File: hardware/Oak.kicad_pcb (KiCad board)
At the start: 2 copper layers, 47 parts, among them J1 18650 Battery holder, J2 USB_B_Micro, J3 Conn_Coaxial, J4 Conn_ARM_JTAG_SWD_10, J5 Conn_01x12_Male, J6 Conn_01x12_Male, SW1 SW_SPDT, SW2 SW_Push, U1 AP2112, U2 ATSAMD21, U3 MCP7383, U4 PA1010D, U5 RFM95, U6 Waveshare_1in54_epaper

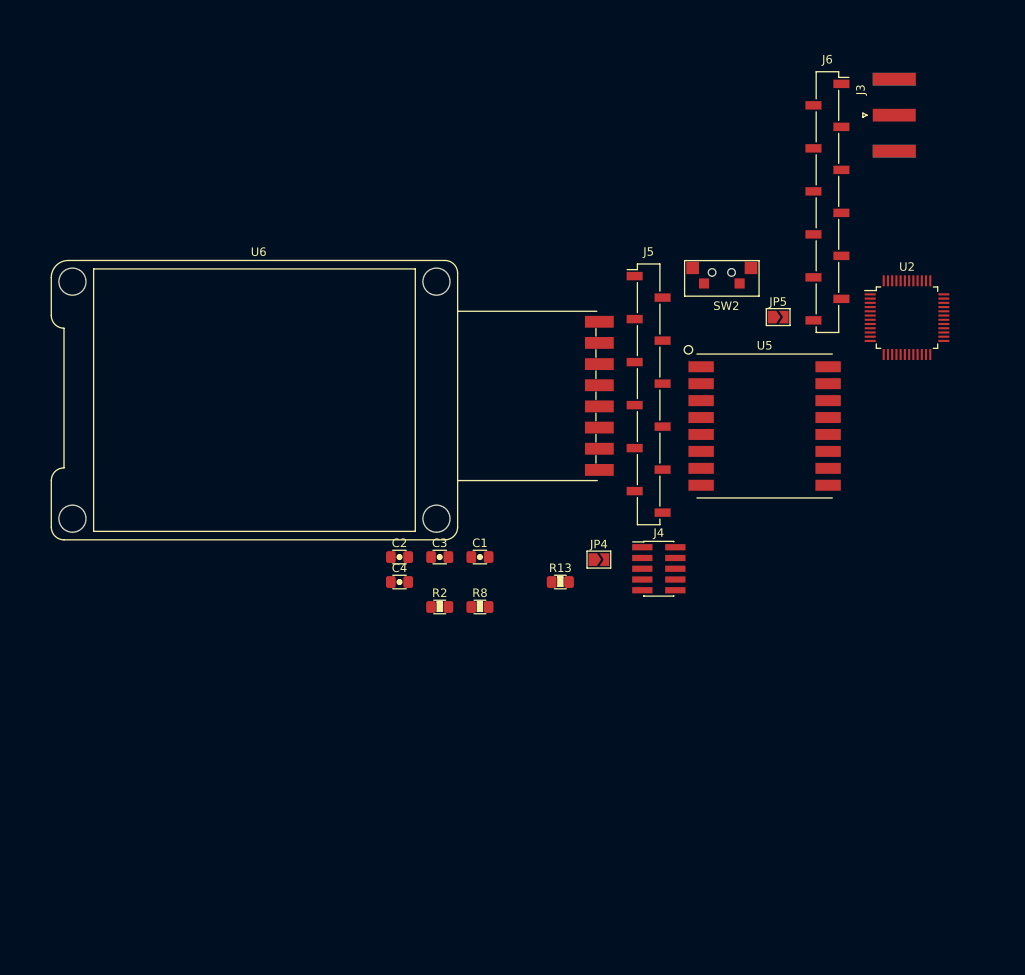
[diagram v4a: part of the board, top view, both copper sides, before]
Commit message: feat: move logical block lora components into a seperate block
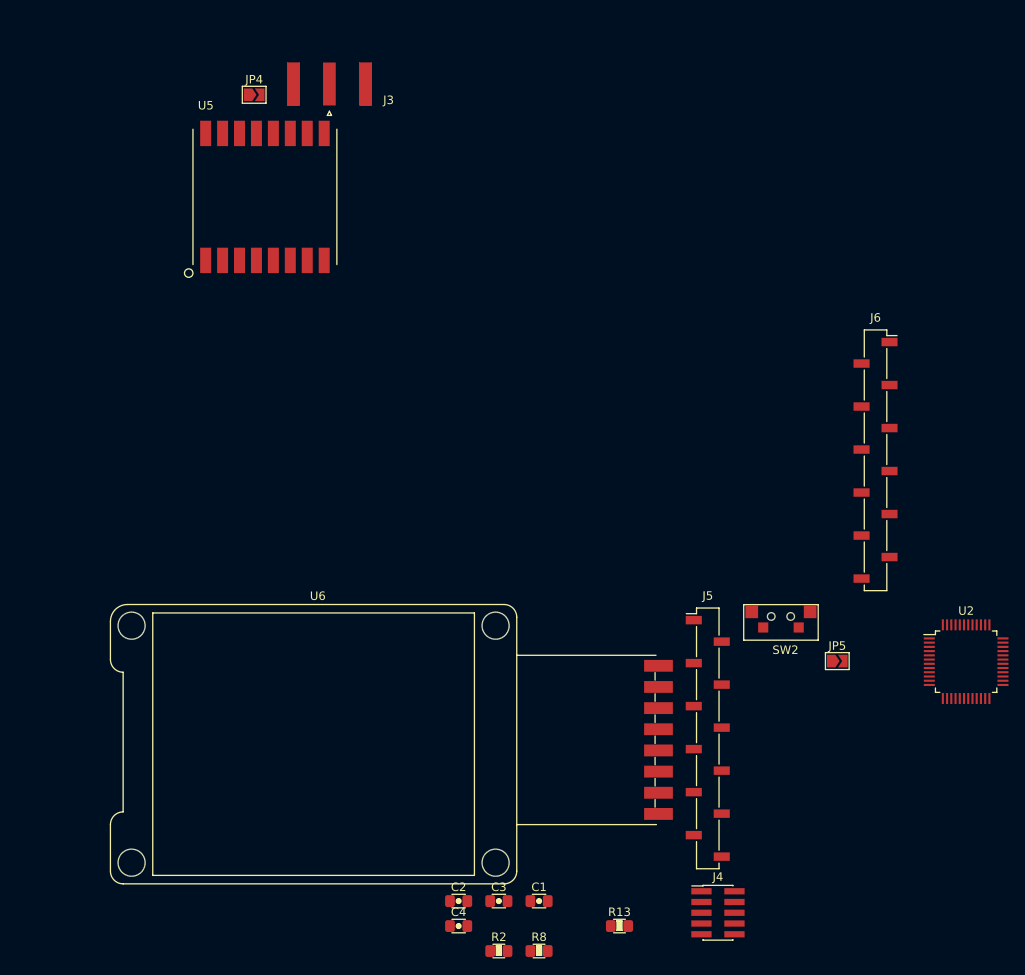
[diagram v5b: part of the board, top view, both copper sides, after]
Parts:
- moved JP4 68.4 mm to (132.1, 53.3)
- moved J3 66.8 mm to (141.0, 52.1), turned to 90 degrees
- moved U5 64.9 mm to (133.3, 65.4), turned to 90 degrees
- moved R2 41.2 mm to (161.0, 154.5)
- moved R8 41.2 mm to (165.7, 154.5)
- moved C1 41.2 mm to (165.7, 148.6)
- moved C2 41.2 mm to (156.2, 148.6)
- moved C3 41.2 mm to (161.0, 148.6)
- moved J4 41.2 mm to (186.9, 150.0)
- moved JP5 41.2 mm to (201.0, 120.2)
- moved SW2 41.2 mm to (194.3, 115.0)
- moved U2 41.2 mm to (216.2, 120.3)
- moved J5 41.2 mm to (185.7, 129.4)
- moved U6 41.2 mm to (139.6, 129.6)
- moved C4 41.2 mm to (156.2, 151.5)
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
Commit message: feat: move logical block eink components into a seperate block
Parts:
- moved U6 126.1 mm to (265.4, 121.9)
- moved JP5 93.6 mm to (293.4, 135.3)
- moved J1 18.5 mm to (75.6, 28.6)

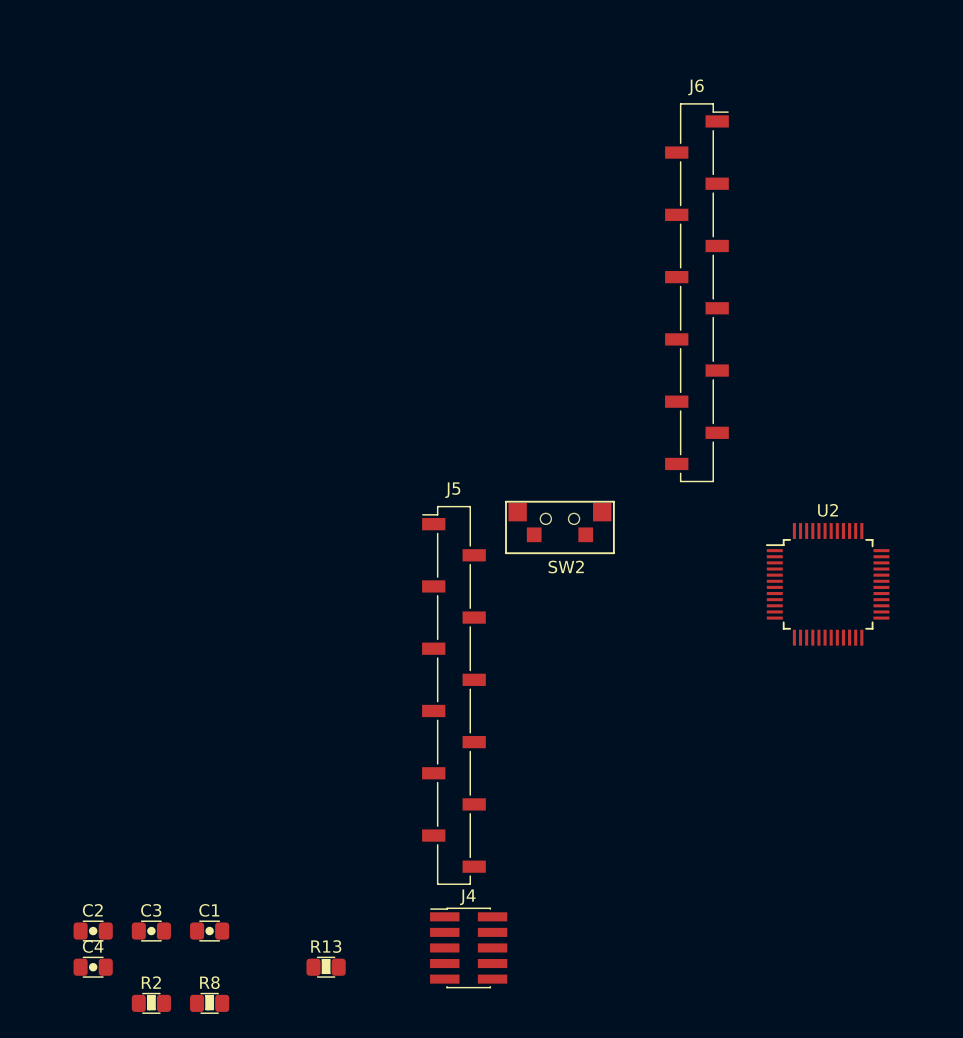
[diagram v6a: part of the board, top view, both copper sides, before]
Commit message: feat: move logical block mcu components into a seperate block
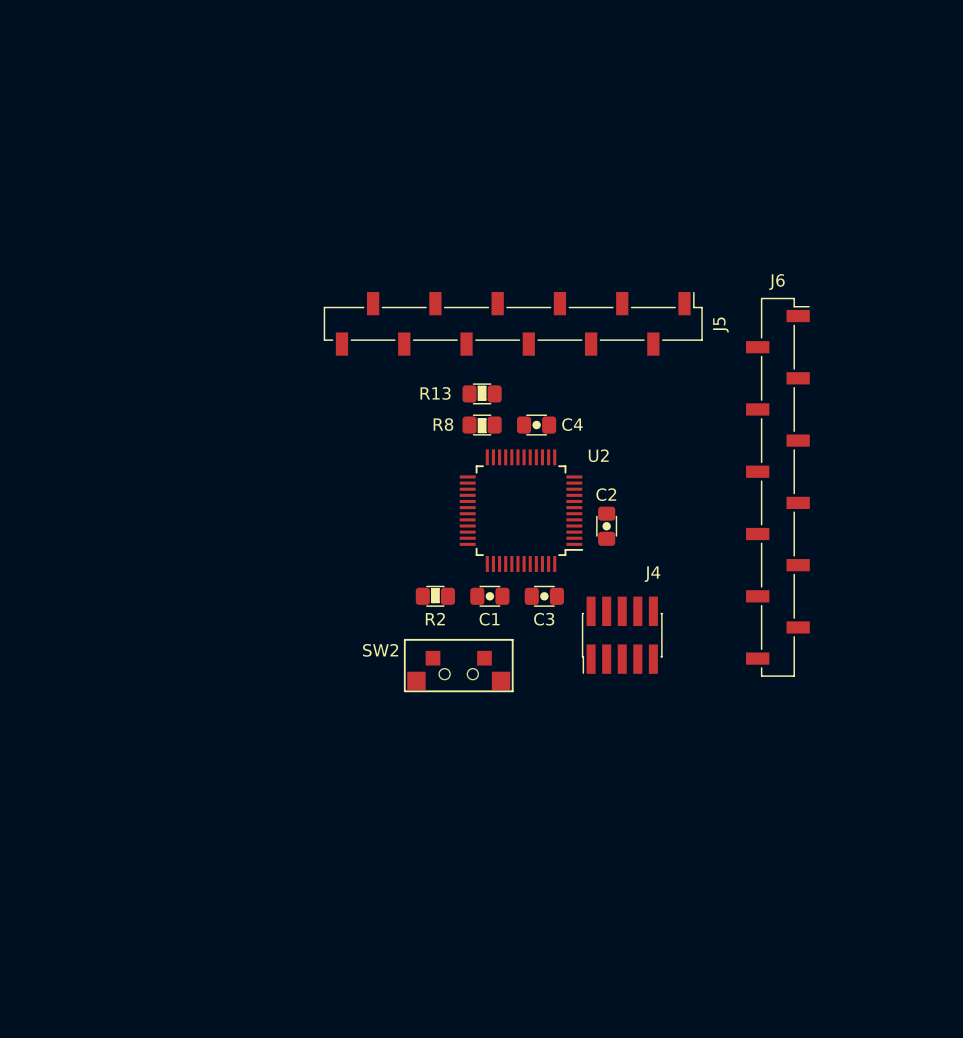
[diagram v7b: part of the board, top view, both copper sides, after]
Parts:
- moved C4 57.1 mm to (192.4, 107.3), turned to 180 degrees
- moved C2 53.3 mm to (198.1, 115.6), turned to 270 degrees
- moved R8 52.1 mm to (188.0, 107.3), turned to 180 degrees
- moved R13 48.5 mm to (188.0, 104.8)
- moved C3 42.1 mm to (193.0, 121.3)
- moved R2 40.5 mm to (184.2, 121.3)
- moved C1 35.6 mm to (188.6, 121.3)
- moved J5 30.7 mm to (190.5, 99.1), turned to 270 degrees
- moved J4 28.4 mm to (199.4, 124.5), turned to 90 degrees
- moved U2 25.8 mm to (191.1, 114.3), turned to 180 degrees
- moved J6 17.2 mm to (212.1, 112.4)
- moved SW2 15.1 mm to (186.1, 127.6), turned to 180 degrees

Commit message: feat: move all components nearer
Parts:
- moved D3 180.8 mm to (214.0, 76.8)
- moved R4 180.8 mm to (214.0, 73.0)
- moved R7 180.8 mm to (214.0, 80.6)
- moved U4 180.8 mm to (203.8, 76.8)
- moved JP3 178.5 mm to (193.6, 80.0), turned to 0 degrees
- moved R12 174.4 mm to (193.7, 73.7), turned to 0 degrees
- moved J1 105.7 mm to (154.9, 98.4)
- moved R6 93.1 mm to (121.3, 113.0), turned to 270 degrees
- moved D5 90.3 mm to (118.7, 113.0), turned to 270 degrees
- moved JP5 87.8 mm to (208.3, 113.7)
- moved U6 87.8 mm to (180.3, 100.3)
- moved D4 87.4 mm to (116.2, 113.0), turned to 270 degrees
- moved R3 87.2 mm to (109.2, 106.7), turned to 180 degrees
- moved J2 85.0 mm to (101.0, 92.1)
- moved R11 85.0 mm to (128.3, 106.7)
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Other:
- board text removed: "2 Traces out: GPS_DATA, GPS_RST 1 LED: D3"
- board text removed: "3 decaps: C10, C6, C7 4 Traces out: VBUS, VBATT, USB D+/D- 2 connectors: uUSB, Switch"
- board text removed: "3 decaps: C11, C5, C9 2 Traces out: VBUS, VBAT 1 LED"
